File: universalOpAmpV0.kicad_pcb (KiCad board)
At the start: 4 copper layers, 19 parts, among them SW3 218-4LPSTR, SW4 SW_DPDT, SW5 SW_DPDT, SW6 CS-4-14, SW7 SW_SP3T, SW8 218-8LPSTR, U1 OPA992DBV

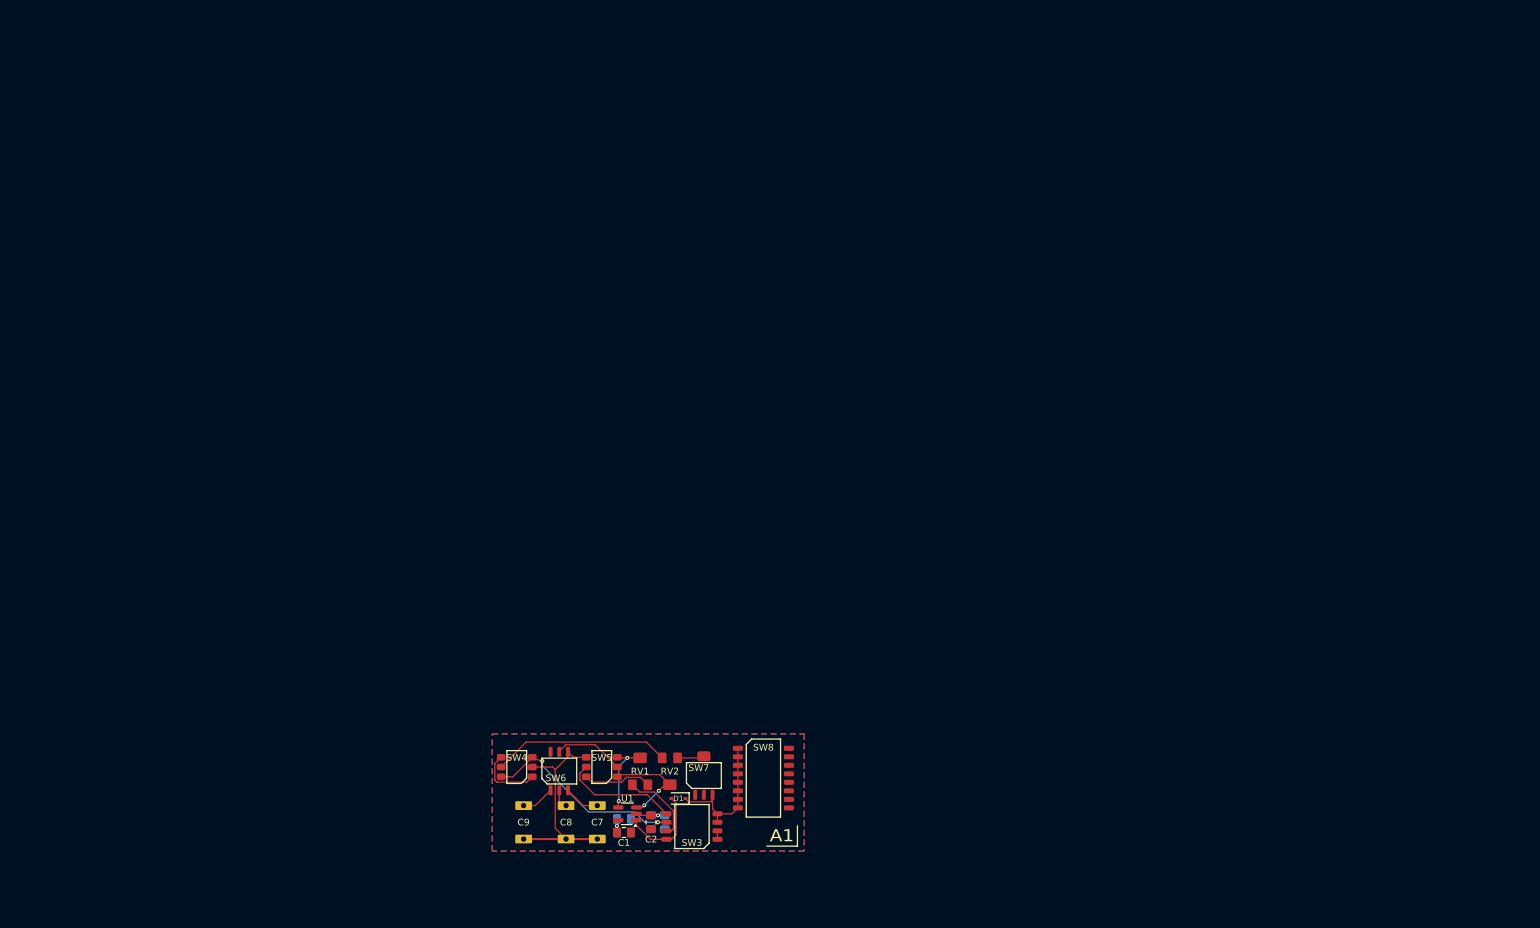
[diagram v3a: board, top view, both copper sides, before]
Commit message: preliminary layout of op amp blocks complete
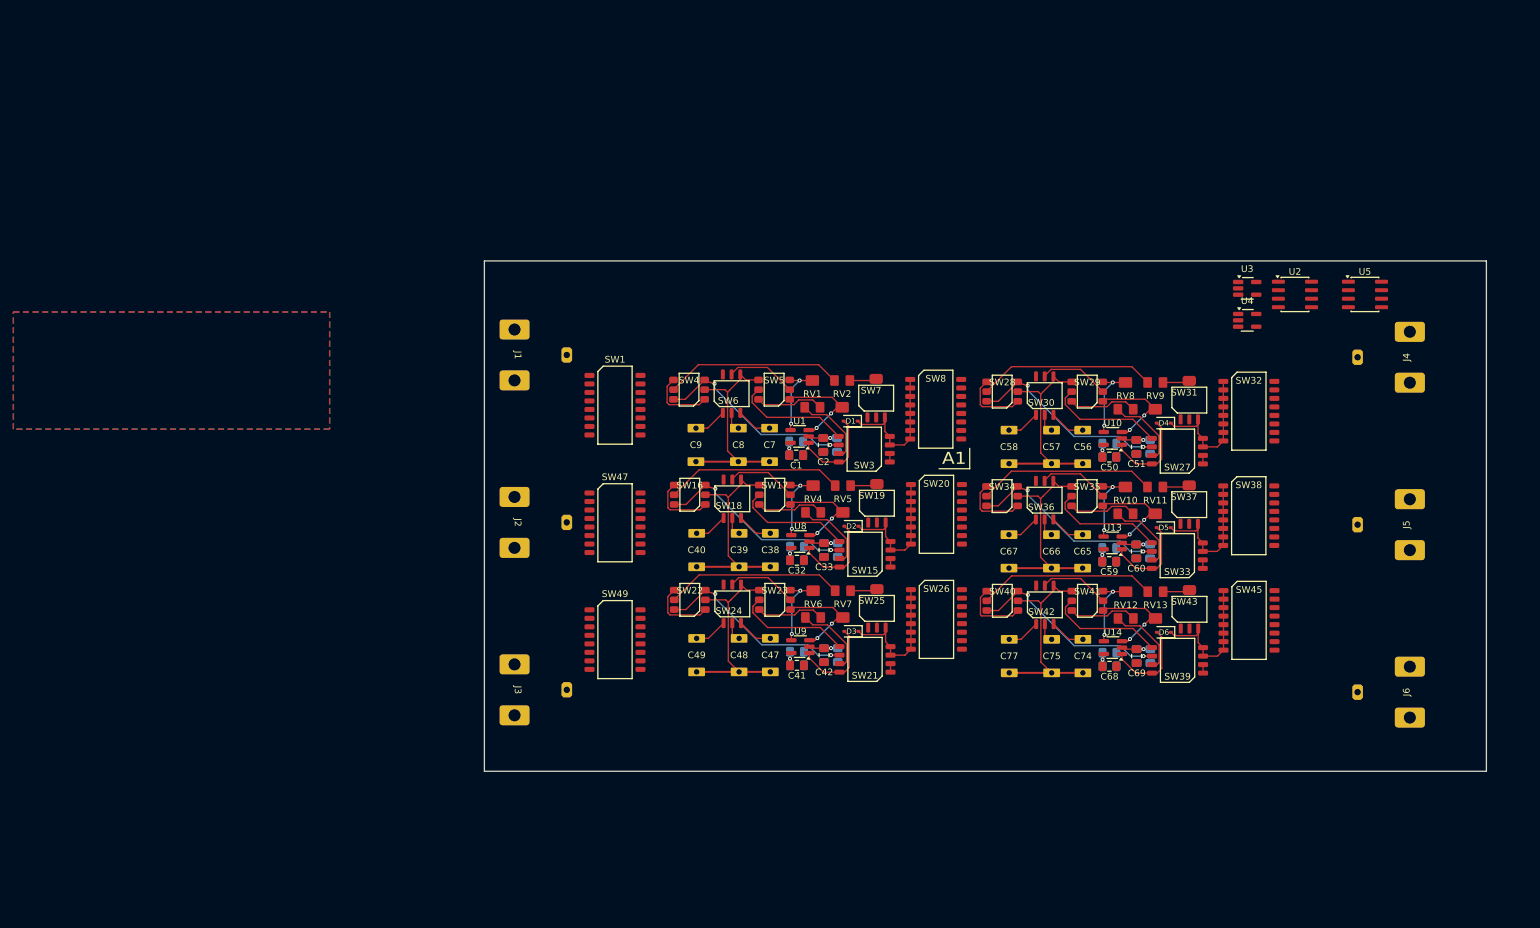
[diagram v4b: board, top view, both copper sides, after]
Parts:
- added C32: C, uniOpAmpLib:C_0805_Metric2012_HandSolder, F.Cu at (142.2, 105.7)
- added C33: C, uniOpAmpLib:C_0805_Metric2012_HandSolder, F.Cu at (146.2, 104.1)
- added C34: C, uniOpAmpLib:C_0805_Metric2012_HandSolder, B.Cu at (142.2, 103.6)
- added C35: C, uniOpAmpLib:C_0805_Metric2012_HandSolder, B.Cu at (146.2, 104.1)
- added C36: C, uniOpAmpLib:C_0805_Metric2012_HandSolder, B.Cu at (142.2, 105.7)
- added C37: C, uniOpAmpLib:C_0805_Metric2012_HandSolder, B.Cu at (148.3, 104.1)
- added C38: C_Small, uniOpAmpLib:PP_CAP, F.Cu at (138.2, 104.1)
- added C39: C_Small, uniOpAmpLib:PP_CAP, F.Cu at (133.5, 104.1)
- added C40: C_Small, uniOpAmpLib:PP_CAP, F.Cu at (127.2, 104.1)
- added C41: C, uniOpAmpLib:C_0805_Metric2012_HandSolder, F.Cu at (142.2, 121.3)
- added C42: C, uniOpAmpLib:C_0805_Metric2012_HandSolder, F.Cu at (146.2, 119.8)
- added C43: C, uniOpAmpLib:C_0805_Metric2012_HandSolder, B.Cu at (142.2, 119.3)
- added C44: C, uniOpAmpLib:C_0805_Metric2012_HandSolder, B.Cu at (146.2, 119.8)
- added C45: C, uniOpAmpLib:C_0805_Metric2012_HandSolder, B.Cu at (142.2, 121.3)
- added C46: C, uniOpAmpLib:C_0805_Metric2012_HandSolder, B.Cu at (148.3, 119.8)
- added C47: C_Small, uniOpAmpLib:PP_CAP, F.Cu at (138.2, 119.8)
- added C48: C_Small, uniOpAmpLib:PP_CAP, F.Cu at (133.5, 119.8)
- added C49: C_Small, uniOpAmpLib:PP_CAP, F.Cu at (127.2, 119.8)
- added C50: C, uniOpAmpLib:C_0805_Metric2012_HandSolder, F.Cu at (188.8, 90.2)
- added C51: C, uniOpAmpLib:C_0805_Metric2012_HandSolder, F.Cu at (192.9, 88.7)
- added C52: C, uniOpAmpLib:C_0805_Metric2012_HandSolder, B.Cu at (188.8, 88.2)
- added C53: C, uniOpAmpLib:C_0805_Metric2012_HandSolder, B.Cu at (192.9, 88.7)
- added C54: C, uniOpAmpLib:C_0805_Metric2012_HandSolder, B.Cu at (188.8, 90.2)
- added C55: C, uniOpAmpLib:C_0805_Metric2012_HandSolder, B.Cu at (194.9, 88.7)
- added C56: C_Small, uniOpAmpLib:PP_CAP, F.Cu at (184.8, 88.7)
- added C57: C_Small, uniOpAmpLib:PP_CAP, F.Cu at (180.2, 88.7)
- added C58: C_Small, uniOpAmpLib:PP_CAP, F.Cu at (173.8, 88.7)
- added C59: C, uniOpAmpLib:C_0805_Metric2012_HandSolder, F.Cu at (188.8, 105.9)
- added C60: C, uniOpAmpLib:C_0805_Metric2012_HandSolder, F.Cu at (192.8, 104.3)
- added C61: C, uniOpAmpLib:C_0805_Metric2012_HandSolder, B.Cu at (188.8, 103.8)
- added C62: C, uniOpAmpLib:C_0805_Metric2012_HandSolder, B.Cu at (192.8, 104.3)
- added C63: C, uniOpAmpLib:C_0805_Metric2012_HandSolder, B.Cu at (188.8, 105.9)
- added C64: C, uniOpAmpLib:C_0805_Metric2012_HandSolder, B.Cu at (194.9, 104.3)
- added C65: C_Small, uniOpAmpLib:PP_CAP, F.Cu at (184.8, 104.3)
- added C66: C_Small, uniOpAmpLib:PP_CAP, F.Cu at (180.2, 104.3)
- added C67: C_Small, uniOpAmpLib:PP_CAP, F.Cu at (173.8, 104.3)
- added C68: C, uniOpAmpLib:C_0805_Metric2012_HandSolder, F.Cu at (188.8, 121.5)
- added C69: C, uniOpAmpLib:C_0805_Metric2012_HandSolder, F.Cu at (192.9, 120.0)
- added C70: C, uniOpAmpLib:C_0805_Metric2012_HandSolder, B.Cu at (188.8, 119.5)
- added C71: C, uniOpAmpLib:C_0805_Metric2012_HandSolder, B.Cu at (192.9, 120.0)
- added C72: C, uniOpAmpLib:C_0805_Metric2012_HandSolder, B.Cu at (188.8, 121.5)
- added C73: C, uniOpAmpLib:C_0805_Metric2012_HandSolder, B.Cu at (194.9, 120.0)
- added C74: C_Small, uniOpAmpLib:PP_CAP, F.Cu at (184.9, 120.0)
- added C75: C_Small, uniOpAmpLib:PP_CAP, F.Cu at (180.2, 120.0)
- added C77: C_Small, uniOpAmpLib:PP_CAP, F.Cu at (173.9, 120.0)
- added D2: 1N4148WS, Diode_SMD:D_SOD-323, F.Cu at (150.3, 100.6)
- added D3: 1N4148WS, Diode_SMD:D_SOD-323, F.Cu at (150.3, 116.3)
- added D4: 1N4148WS, Diode_SMD:D_SOD-323, F.Cu at (196.9, 85.2)
- added D5: 1N4148WS, Diode_SMD:D_SOD-323, F.Cu at (196.9, 100.8)
- added D6: 1N4148WS, Diode_SMD:D_SOD-323, F.Cu at (197.0, 116.4)
- added J1: BNC I1, uniOpAmpLib:BNC-0731000105, F.Cu at (100.0, 75.0)
- added J2: BNC I1, uniOpAmpLib:BNC-0731000105, F.Cu at (100.0, 100.0)
- added J3: BNC I1, uniOpAmpLib:BNC-0731000105, F.Cu at (100.0, 125.0)
- added J4: BNC I1, uniOpAmpLib:BNC-0731000105, F.Cu at (233.7, 75.3)
- added J5: BNC I1, uniOpAmpLib:BNC-0731000105, F.Cu at (233.7, 100.3)
- added J6: BNC I1, uniOpAmpLib:BNC-0731000105, F.Cu at (233.7, 125.3)
- added RV10: R_Trim_Pot, uniOpAmpLib:PVG5H, F.Cu at (191.2, 96.7)
- added RV11: R_Trim_Pot, uniOpAmpLib:PVG5H, F.Cu at (195.7, 96.7)
- added RV12: R_Trim_Pot, uniOpAmpLib:PVG5H, F.Cu at (191.3, 112.3)
- added RV13: R_Trim_Pot, uniOpAmpLib:PVG5H, F.Cu at (195.7, 112.3)
- added RV4: R_Trim_Pot, uniOpAmpLib:PVG5H, F.Cu at (144.6, 96.5)
- added RV5: R_Trim_Pot, uniOpAmpLib:PVG5H, F.Cu at (149.0, 96.5)
- added RV6: R_Trim_Pot, uniOpAmpLib:PVG5H, F.Cu at (144.6, 112.2)
- added RV7: R_Trim_Pot, uniOpAmpLib:PVG5H, F.Cu at (149.0, 112.2)
- added RV8: R_Trim_Pot, uniOpAmpLib:PVG5H, F.Cu at (191.2, 81.1)
- added RV9: R_Trim_Pot, uniOpAmpLib:PVG5H, F.Cu at (195.7, 81.1)
- added SW1: 218-8LPSTR, uniOpAmpLib:218-8LPSTR, F.Cu at (115.0, 82.5)
- added SW15: 218-4LPSTR, uniOpAmpLib:218-4LPSTR, F.Cu at (152.3, 104.8)
- added SW16: SW_DPDT, uniOpAmpLib:CAS-DxxB, F.Cu at (126.2, 95.9)
- added SW17: SW_DPDT, uniOpAmpLib:CAS-DxxB, F.Cu at (138.9, 95.9)
- added SW18: CS-4-14, uniOpAmpLib:CS-4-14NB, F.Cu at (132.5, 96.5)
- added SW19: SW_SP3T, uniOpAmpLib:CS-4-13NB, F.Cu at (154.1, 97.1)
- added SW20: 218-8LPSTR, uniOpAmpLib:218-8LPSTR, F.Cu at (163.0, 98.8)
- added SW21: 218-4LPSTR, uniOpAmpLib:218-4LPSTR, F.Cu at (152.3, 120.5)
- added SW22: SW_DPDT, uniOpAmpLib:CAS-DxxB, F.Cu at (126.2, 111.6)
- added SW23: SW_DPDT, uniOpAmpLib:CAS-DxxB, F.Cu at (138.9, 111.6)
- added SW24: CS-4-14, uniOpAmpLib:CS-4-14NB, F.Cu at (132.5, 112.2)
- added SW25: SW_SP3T, uniOpAmpLib:CS-4-13NB, F.Cu at (154.1, 112.8)
- added SW26: 218-8LPSTR, uniOpAmpLib:218-8LPSTR, F.Cu at (163.0, 114.5)
- added SW27: 218-4LPSTR, uniOpAmpLib:218-4LPSTR, F.Cu at (199.0, 89.4)
- added SW28: SW_DPDT, uniOpAmpLib:CAS-DxxB, F.Cu at (172.8, 80.5)
- added SW29: SW_DPDT, uniOpAmpLib:CAS-DxxB, F.Cu at (185.5, 80.5)
- added SW30: CS-4-14, uniOpAmpLib:CS-4-14NB, F.Cu at (179.2, 81.1)
- added SW31: SW_SP3T, uniOpAmpLib:CS-4-13NB, F.Cu at (200.8, 81.7)
- added SW32: 218-8LPSTR, uniOpAmpLib:218-8LPSTR, F.Cu at (209.6, 83.4)
- added SW33: 218-4LPSTR, uniOpAmpLib:218-4LPSTR, F.Cu at (199.0, 105.0)
- added SW34: SW_DPDT, uniOpAmpLib:CAS-DxxB, F.Cu at (172.8, 96.1)
- added SW35: SW_DPDT, uniOpAmpLib:CAS-DxxB, F.Cu at (185.5, 96.1)
- added SW36: CS-4-14, uniOpAmpLib:CS-4-14NB, F.Cu at (179.1, 96.7)
- added SW37: SW_SP3T, uniOpAmpLib:CS-4-13NB, F.Cu at (200.7, 97.3)
- added SW38: 218-8LPSTR, uniOpAmpLib:218-8LPSTR, F.Cu at (209.6, 99.0)
- added SW39: 218-4LPSTR, uniOpAmpLib:218-4LPSTR, F.Cu at (199.0, 120.6)
- added SW40: SW_DPDT, uniOpAmpLib:CAS-DxxB, F.Cu at (172.8, 111.7)
- added SW41: SW_DPDT, uniOpAmpLib:CAS-DxxB, F.Cu at (185.5, 111.7)
- added SW42: CS-4-14, uniOpAmpLib:CS-4-14NB, F.Cu at (179.2, 112.3)
- added SW43: SW_SP3T, uniOpAmpLib:CS-4-13NB, F.Cu at (200.8, 113.0)
- added SW45: 218-8LPSTR, uniOpAmpLib:218-8LPSTR, F.Cu at (209.7, 114.6)
- added SW47: 218-8LPSTR, uniOpAmpLib:218-8LPSTR, F.Cu at (115.0, 100.1)
- added SW49: 218-8LPSTR, uniOpAmpLib:218-8LPSTR, F.Cu at (115.0, 117.5)
- added U10: OPA992DBV, uniOpAmpLib:SOT-23-5_HandSoldering, F.Cu at (189.3, 87.5)
- added U13: OPA992DBV, uniOpAmpLib:SOT-23-5_HandSoldering, F.Cu at (189.3, 103.1)
- added U14: OPA992DBV, uniOpAmpLib:SOT-23-5_HandSoldering, F.Cu at (189.3, 118.7)
- added U2: BUF634A, Package_SO:SOIC-8_3.9x4.9mm_P1.27mm, F.Cu at (216.5, 66.0)
- added U3: OPA992DBV, Package_TO_SOT_SMD:SOT-23-5_HandSoldering, F.Cu at (209.4, 65.1)
- added U4: OPA992DBV, Package_TO_SOT_SMD:SOT-23-5_HandSoldering, F.Cu at (209.4, 69.8)
- added U5: BUF634A, Package_SO:SOIC-8_3.9x4.9mm_P1.27mm, F.Cu at (227.0, 66.0)
- added U8: OPA992DBV, uniOpAmpLib:SOT-23-5_HandSoldering, F.Cu at (142.7, 102.9)
- added U9: OPA992DBV, uniOpAmpLib:SOT-23-5_HandSoldering, F.Cu at (142.7, 118.5)
- moved C1 61.9 mm to (142.1, 90.0)
- moved C2 61.9 mm to (146.1, 88.4)
- moved C4 61.9 mm to (146.1, 88.4)
- moved C5 61.9 mm to (142.1, 90.0)
- moved C6 61.9 mm to (148.2, 88.4)
- moved C7 61.9 mm to (138.1, 88.4)
- moved C8 61.9 mm to (133.4, 88.4)
- moved C9 61.9 mm to (127.1, 88.4)
- moved RV2 61.9 mm to (148.9, 80.8)
- moved SW4 61.9 mm to (126.1, 80.2)
- moved C3 61.9 mm to (142.1, 87.9)
- moved D1 61.9 mm to (150.2, 84.9)
- moved RV1 61.9 mm to (144.5, 80.8)
- moved SW3 61.9 mm to (152.2, 89.1)
- moved SW5 61.9 mm to (138.8, 80.2)
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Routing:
- net Net-(C74-Pad1): track 0.00 -> 32.1 mm
- net Net-(C47-Pad1): track 0.00 -> 32.1 mm
- net Net-(C65-Pad1): track 0.00 -> 32.1 mm
- net Net-(C38-Pad1): track 0.00 -> 32.1 mm
- net Net-(C56-Pad1): track 0.00 -> 32.1 mm
- net -VDC: track 6.14 -> 36.9 mm, vias 1 -> 6
- net Net-(SW33B-O): track 0.00 -> 30.4 mm, vias 0 -> 2
- net Net-(SW27B-O): track 0.00 -> 30.4 mm, vias 0 -> 2
- net Net-(SW21B-O): track 0.00 -> 30.4 mm, vias 0 -> 2
- net Net-(SW15B-O): track 0.00 -> 30.4 mm, vias 0 -> 2
- net Net-(SW39B-O): track 0.00 -> 30.4 mm, vias 0 -> 2
- net Net-(RV9-Pad1): track 0.00 -> 26.6 mm
- net Net-(RV5-Pad1): track 0.00 -> 26.6 mm
- net Net-(RV11-Pad1): track 0.00 -> 26.6 mm
- net Net-(RV13-Pad1): track 0.00 -> 26.6 mm
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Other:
- board outline added: 149.6 x 76.2 mm

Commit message: initial interconnect bus layout complete, board changed to 6 layers due to bus layer requirements
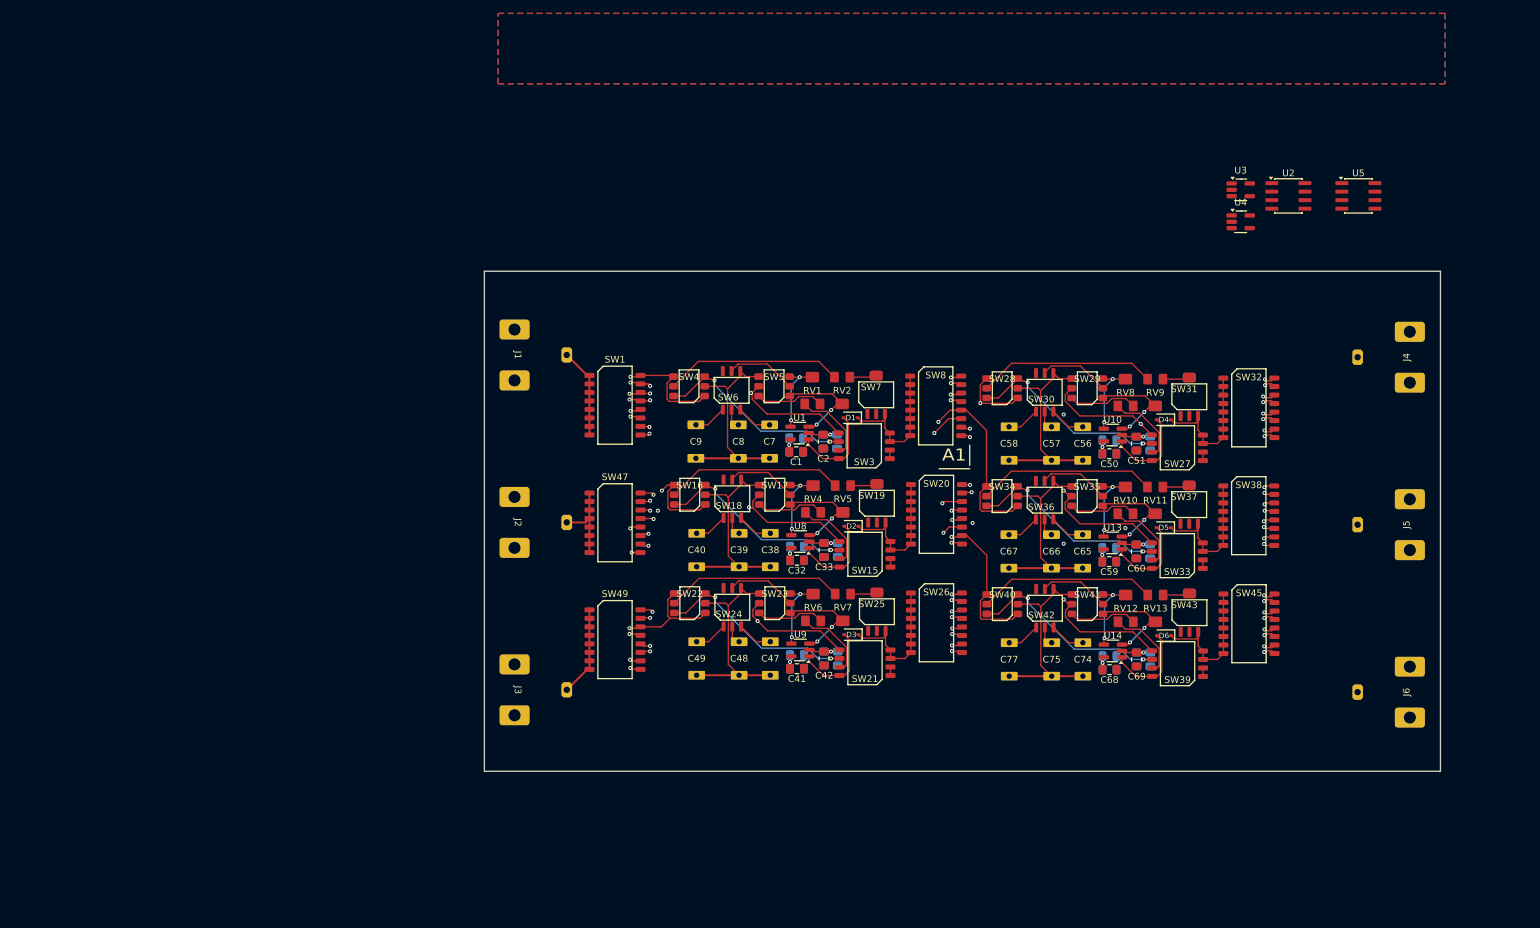
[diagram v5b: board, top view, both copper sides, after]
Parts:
- moved U3 14.7 mm to (208.4, 50.3)
- moved U2 14.7 mm to (215.6, 51.2)
- moved U5 14.7 mm to (226.0, 51.2)
- moved U4 14.7 mm to (208.4, 55.1)
- moved C1 0.50 mm to (142.1, 89.5)
- moved C2 0.50 mm to (146.1, 87.9)
- moved C3 0.50 mm to (142.1, 87.4)
- moved C4 0.50 mm to (146.1, 87.9)
- moved C41 0.50 mm to (142.2, 121.8)
- moved C42 0.50 mm to (146.2, 120.3)
- moved C43 0.50 mm to (142.2, 119.8)
- moved C44 0.50 mm to (146.2, 120.3)
- moved C45 0.50 mm to (142.2, 121.8)
- moved C46 0.50 mm to (148.3, 120.3)
- moved C47 0.50 mm to (138.2, 120.3)
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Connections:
- SW1 pad 10: P4 -> P5
- SW1 pad 11: P2 -> N4
- SW1 pad 12: P1 -> P4
- SW1 pad 13: N5 -> N2
- SW1 pad 14: N4 -> P2
- SW1 pad 15: N2 -> N1
- SW1 pad 16: N1 -> P1
- SW1 pad 9: P5 -> N5
- SW20 pad 11: P1 -> N4
- SW20 pad 12: P3 -> P4
- SW20 pad 13: N4 -> N3
- SW20 pad 14: N6 -> P3
- SW20 pad 16: N3 -> P1
- SW20 pad 9: P4 -> N6
- SW26 pad 10: P4 -> P5
- SW26 pad 11: P2 -> N4
- SW26 pad 12: P1 -> P4
- SW26 pad 13: N5 -> N2
- SW26 pad 14: N4 -> P2
- SW26 pad 15: N2 -> N1
- SW26 pad 16: N1 -> P1
- SW26 pad 9: P5 -> N5
- SW32 pad 10: P5 -> P6
- SW32 pad 11: P3 -> N5
- SW32 pad 12: P2 -> P5
- SW32 pad 13: N6 -> N3
- SW32 pad 14: N5 -> P3
- SW32 pad 15: N3 -> N2
- SW32 pad 16: N2 -> P2
- SW32 pad 9: P6 -> N6
- SW38 pad 11: P1 -> N4
- SW38 pad 12: P3 -> P4
- SW38 pad 13: N4 -> N3
- SW38 pad 14: N6 -> P3
- SW38 pad 16: N3 -> P1
- SW38 pad 9: P4 -> N6
- SW45 pad 10: P4 -> P5
- SW45 pad 11: P2 -> N4
- SW45 pad 12: P1 -> P4
- SW45 pad 13: N5 -> N2
- SW45 pad 14: N4 -> P2
- SW45 pad 15: N2 -> N1
- SW45 pad 16: N1 -> P1
- SW45 pad 9: P5 -> N5
- SW47 pad 10: P5 -> P6
- SW47 pad 11: P3 -> N4
- SW47 pad 12: P2 -> P4
- SW47 pad 13: N6 -> N3
- SW47 pad 14: N5 -> P3
- SW47 pad 15: N3 -> N1
- SW47 pad 16: N2 -> P1
- SW47 pad 9: P6 -> N6
- SW49 pad 11: P1 -> N5
- SW49 pad 12: P3 -> P5
- SW49 pad 13: N4 -> N3
- SW49 pad 14: N6 -> P3
- SW49 pad 15: N1 -> N2
- SW49 pad 16: N3 -> P2
- SW49 pad 9: P4 -> N6
- SW8 pad 10: P5 -> P6
- SW8 pad 11: P3 -> N5
- SW8 pad 12: P2 -> P5
- SW8 pad 13: N6 -> N3
- SW8 pad 14: N5 -> P3
- SW8 pad 15: N3 -> N2
- SW8 pad 16: N2 -> P2
- SW8 pad 9: P6 -> N6
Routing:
- net N2: track 17.3 -> 265.6 mm, vias 0 -> 9
- net P5: track 9.87 -> 256.3 mm, vias 0 -> 6
- net N5: track 17.3 -> 263.7 mm, vias 0 -> 8
- net P2: track 9.84 -> 246.8 mm, vias 0 -> 8
- net P4: track 9.84 -> 217.3 mm, vias 0 -> 8
- net N1: track 17.3 -> 222.0 mm, vias 0 -> 8
- net N3: track 17.3 -> 221.9 mm, vias 0 -> 7
- net N4: track 17.3 -> 220.4 mm, vias 0 -> 8
- net N6: track 17.3 -> 213.0 mm, vias 0 -> 8
- net P6: track 9.92 -> 204.8 mm, vias 0 -> 6
- net P3: track 9.84 -> 201.5 mm, vias 0 -> 6
- net P1: track 9.84 -> 200.7 mm, vias 0 -> 6
- net /InputStage3/I: track 0.00 -> 13.5 mm
- net /InputStage1/I: track 0.00 -> 13.5 mm
- net /InputStage2/I: track 0.00 -> 12.5 mm
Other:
- board size 149.6 x 76.2 mm -> 142.8 x 74.7 mm
- copper layers 4 -> 6
